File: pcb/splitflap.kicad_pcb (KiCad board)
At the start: 2 copper layers, 100 x 100 mm, 61 parts, among them J1 Conn_01x05, J10 Hall C, J11 Hall-D, J12 I2C, J2 Conn_01x05, J3 Conn_01x05, J4 Conn_01x05, J5 Barrel_Jack_Switch, J6 USB_C_Receptacle_USB2.0_16P, J7 Barrel_Jack_Switch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

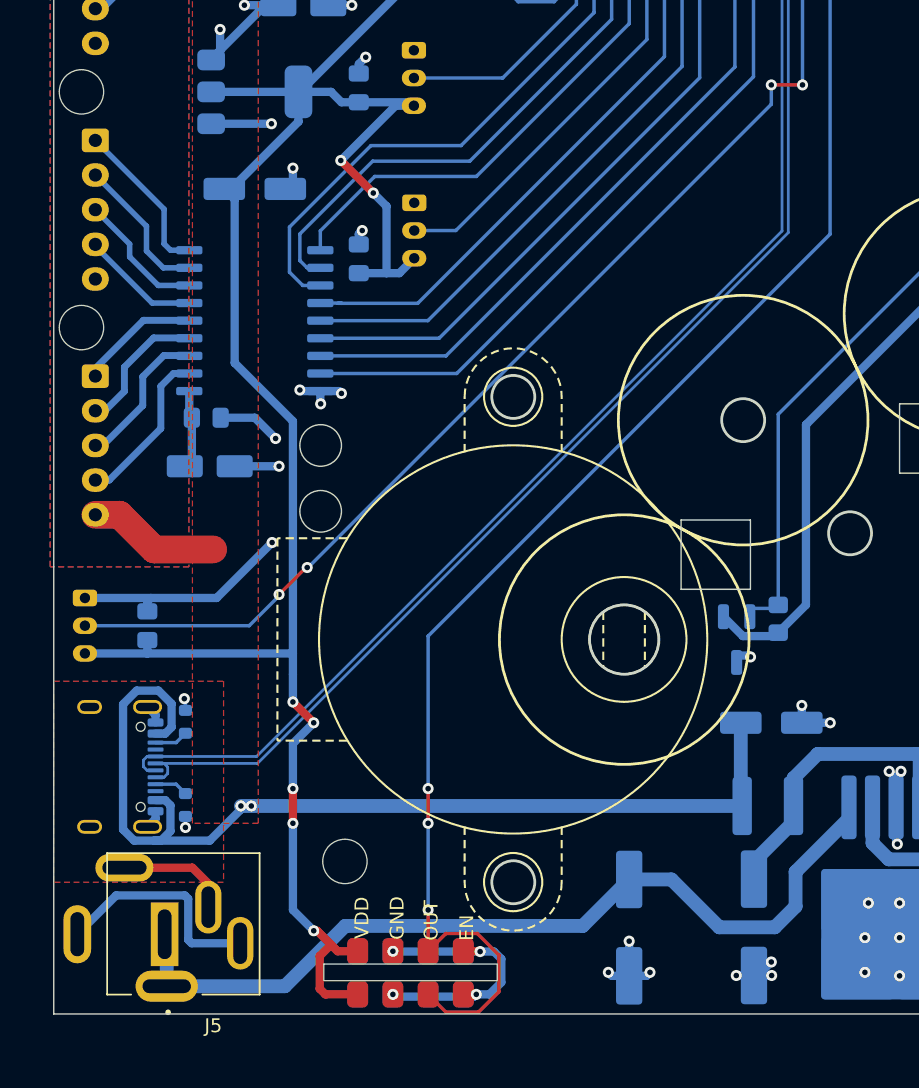
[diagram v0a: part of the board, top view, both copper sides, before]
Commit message: Add optional LED for DCF receiver
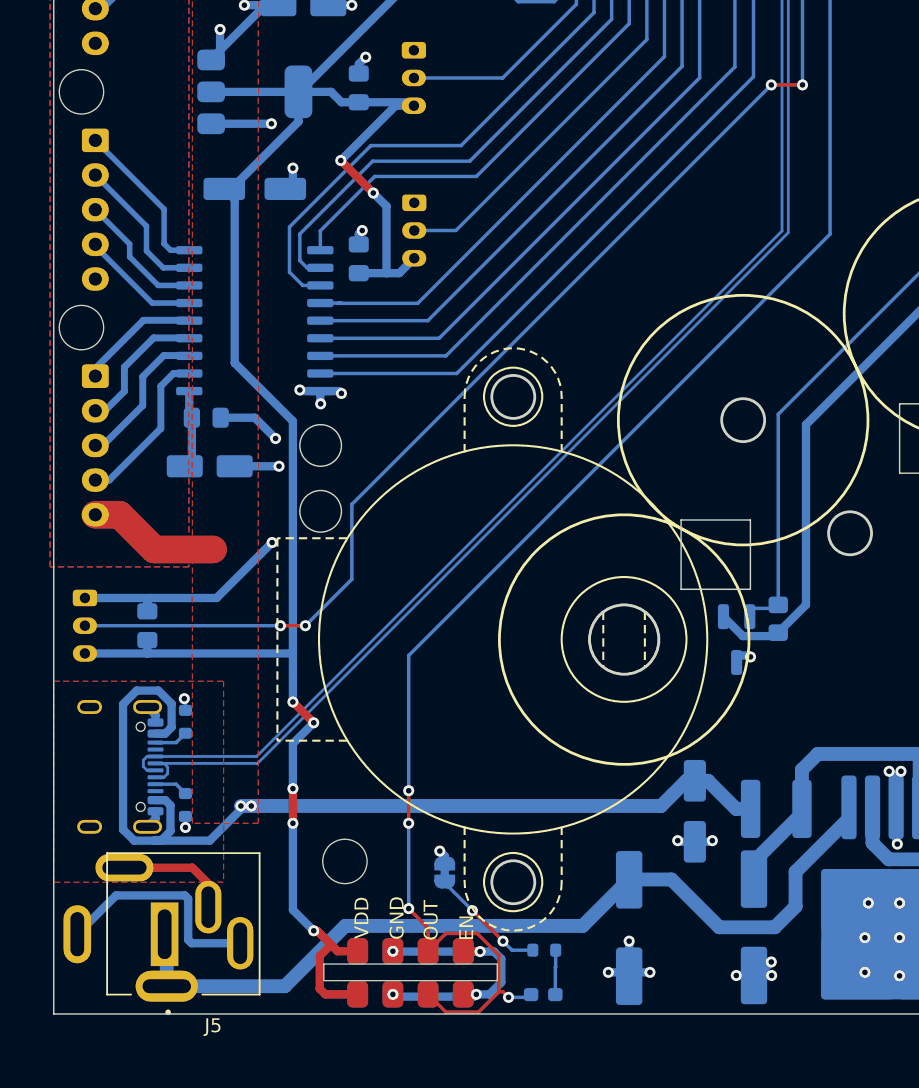
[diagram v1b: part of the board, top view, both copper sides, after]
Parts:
- added D2: LED, LED_SMD:LED_0603_1608Metric_Pad1.05x0.95mm_HandSolder, B.Cu at (135.3, 148.6)
- added JP2: DCF77 LED, Jumper:SolderJumper-2_P1.3mm_Bridged_RoundedPad1.0x1.5mm, B.Cu at (128.2, 139.8)
- added R6: 1k, Resistor_SMD:R_0603_1608Metric, B.Cu at (135.4, 145.4)
- moved C4 8.43 mm to (146.2, 135.4), turned to -90 degrees
- moved L2 0.64 mm to (152.1, 135.2)
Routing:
- net Net-(JP2-B): track 0.00 -> 8.46 mm, vias 0 -> 2
- net +5V: track 111.6 -> 107.7 mm
- net DCF77: track 114.9 -> 118.6 mm, vias 5 -> 6
- net Net-(D2-K): track 0.00 -> 3.21 mm
- net /HALL_A: track 122.8 -> 125.1 mm
- net GND: track 119.1 -> 119.5 mm, vias 53 -> 54

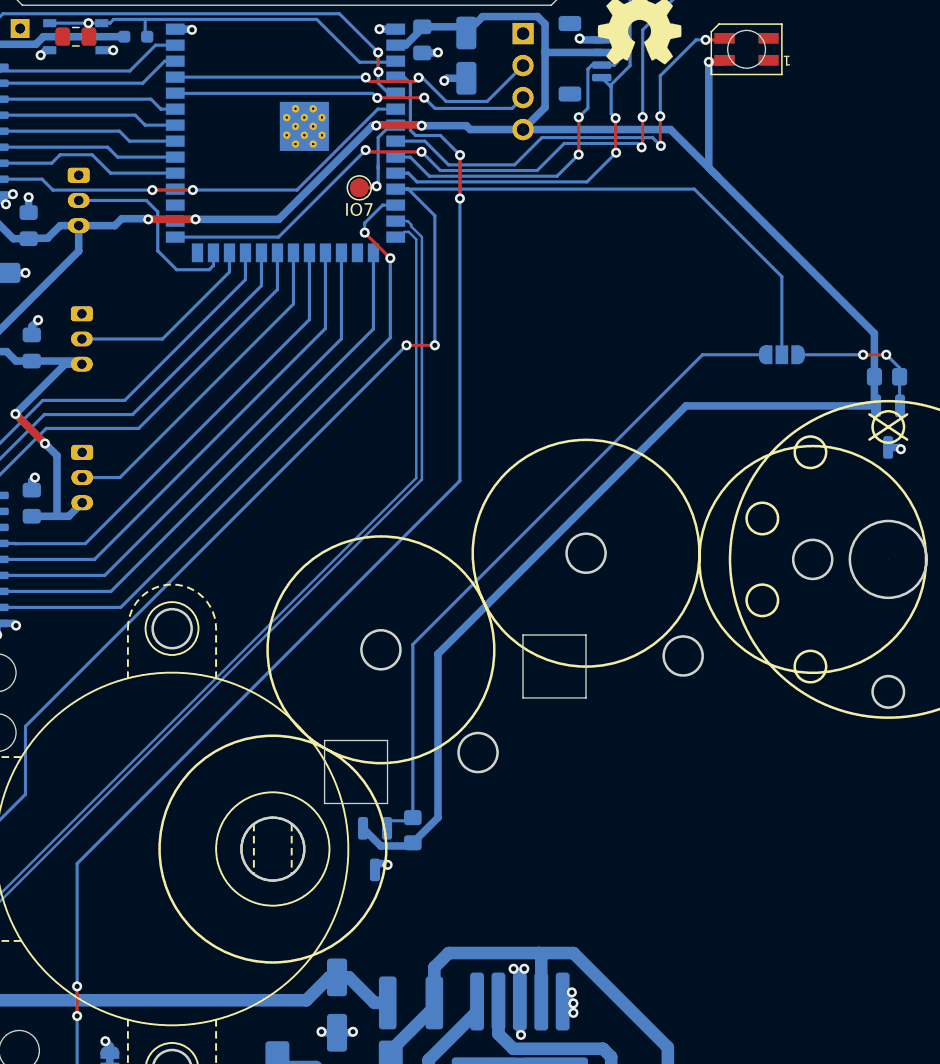
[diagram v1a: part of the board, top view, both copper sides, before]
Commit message: Add two Hall sensors to the current board so that the amount of backlash can be registered
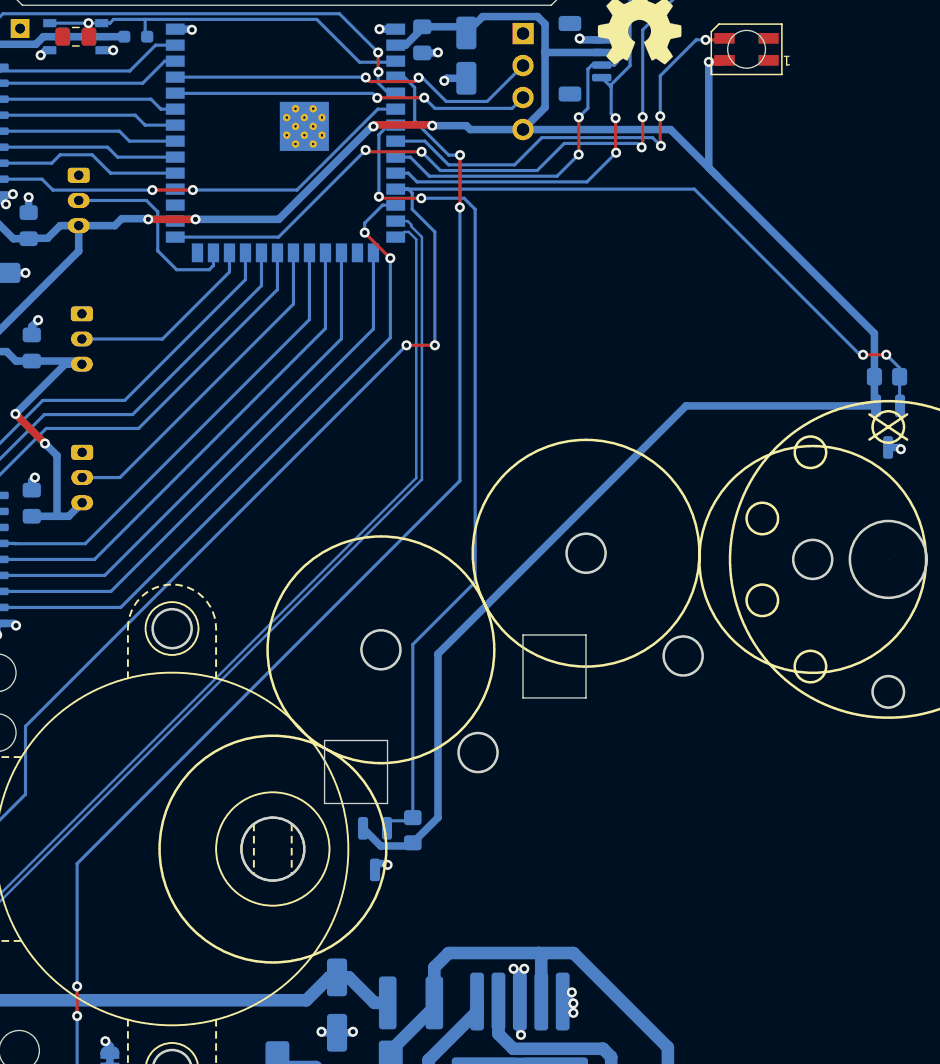
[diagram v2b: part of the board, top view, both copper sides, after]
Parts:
- removed JP1: Hall-A Switch, Jumper:SolderJumper-3_P1.3mm_Open_RoundedPad1.0x1.5mm
- removed TP1: IO7, TestPoint:TestPoint_Pad_D1.5mm
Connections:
- J8 pad 2: /HALL_A -> /HALL_A1
- U4 pad 11: /HALL_A -> /HALL_A1
- U4 pad 7: Extra -> /HALL_A2
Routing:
- net /HALL_A: track 125.1 -> 0.00 mm, vias 4 -> 0
- net /HALL_A1: track 11.5 -> 134.3 mm, vias 2 -> 6
- net /HALL_A2: track 53.5 -> 67.2 mm, vias 0 -> 2
- net Extra: track 7.40 -> 0.00 mm, vias 1 -> 0
- net DCF77: track 118.6 -> 118.0 mm

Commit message: Remapping the motors ABCD to match the connectors on the board
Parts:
- J1: value Conn_01x05 -> Motor D
- J11: value Hall-D -> Hall B
- J2: value Conn_01x05 -> Motor C
- J3: value Conn_01x05 -> Motor B
- J4: value Conn_01x05 -> Motor A
- J8: value Hall A -> Hall A1
- J9: value Hall B -> Hall D
- U5: value AH1815-W-7 -> Hall A1
- U9: value AH1815-W-7 -> Hall A2
- moved OSHW1 16.2 mm to (186.0, 61.6)
- moved C11 0.15 mm to (106.6, 122.0)
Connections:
- J1 pad 1: /MOUT-A1 -> /MOUT-D1
- J1 pad 2: /MOUT-A2 -> /MOUT-D2
- J1 pad 3: /MOUT-A3 -> /MOUT-D3
- J1 pad 4: /MOUT-A4 -> /MOUT-D4
- J11 pad 2: /HALL_D -> /HALL_B
- J2 pad 1: /MOUT-B1 -> /MOUT-C1
- J2 pad 2: /MOUT-B2 -> /MOUT-C2
- J2 pad 3: /MOUT-B3 -> /MOUT-C3
- J2 pad 4: /MOUT-B4 -> /MOUT-C4
- J3 pad 1: /MOUT-C1 -> /MOUT-B1
- J3 pad 2: /MOUT-C2 -> /MOUT-B2
- J3 pad 3: /MOUT-C3 -> /MOUT-B3
- J3 pad 4: /MOUT-C4 -> /MOUT-B4
- J4 pad 1: /MOUT-D1 -> /MOUT-A1
- J4 pad 2: /MOUT-D2 -> /MOUT-A2
- J4 pad 3: /MOUT-D3 -> /MOUT-A3
- J4 pad 4: /MOUT-D4 -> /MOUT-A4
- J9 pad 2: /HALL_B -> /HALL_D
- U1 pad 1: /MOTOR-A-1 -> /MOTOR-D-1
- U1 pad 11: /MOUT-B4 -> /MOUT-C4
- U1 pad 12: /MOUT-B3 -> /MOUT-C3
- U1 pad 13: /MOUT-B2 -> /MOUT-C2
- U1 pad 14: /MOUT-B1 -> /MOUT-C1
- U1 pad 15: /MOUT-A4 -> /MOUT-D4
- U1 pad 16: /MOUT-A3 -> /MOUT-D3
- U1 pad 17: /MOUT-A2 -> /MOUT-D2
- U1 pad 18: /MOUT-A1 -> /MOUT-D1
- U1 pad 2: /MOTOR-A-2 -> /MOTOR-D-2
- U1 pad 3: /MOTOR-A-3 -> /MOTOR-D-3
- U1 pad 4: /MOTOR-A-4 -> /MOTOR-D-4
- U1 pad 5: /MOTOR-B-1 -> /MOTOR-C-1
- U1 pad 6: /MOTOR-B-2 -> /MOTOR-C-2
- U1 pad 7: /MOTOR-B-3 -> /MOTOR-C-3
- U1 pad 8: /MOTOR-B-4 -> /MOTOR-C-4
- U2 pad 1: /MOTOR-C-1 -> /MOTOR-B-1
- U2 pad 11: /MOUT-D4 -> /MOUT-A4
- U2 pad 12: /MOUT-D3 -> /MOUT-A3
- U2 pad 13: /MOUT-D2 -> /MOUT-A2
- U2 pad 14: /MOUT-D1 -> /MOUT-A1
- U2 pad 15: /MOUT-C4 -> /MOUT-B4
- U2 pad 16: /MOUT-C3 -> /MOUT-B3
- U2 pad 17: /MOUT-C2 -> /MOUT-B2
- U2 pad 18: /MOUT-C1 -> /MOUT-B1
- U2 pad 2: /MOTOR-C-2 -> /MOTOR-B-2
- U2 pad 3: /MOTOR-C-3 -> /MOTOR-B-3
- U2 pad 4: /MOTOR-C-4 -> /MOTOR-B-4
- U2 pad 5: /MOTOR-D-1 -> /MOTOR-A-1
- U2 pad 6: /MOTOR-D-2 -> /MOTOR-A-2
- U2 pad 7: /MOTOR-D-3 -> /MOTOR-A-3
- U2 pad 8: /MOTOR-D-4 -> /MOTOR-A-4
- U4 pad 12: /MOTOR-D-4 -> /MOTOR-A-4
- U4 pad 15: /MOTOR-D-3 -> /MOTOR-A-3
- U4 pad 17: /MOTOR-D-2 -> /MOTOR-A-2
- U4 pad 18: /MOTOR-D-1 -> /MOTOR-A-1
- U4 pad 19: /MOTOR-C-4 -> /MOTOR-B-4
- U4 pad 20: /HALL_D -> /HALL_B
- U4 pad 21: /MOTOR-C-1 -> /MOTOR-B-1
- U4 pad 22: /MOTOR-C-2 -> /MOTOR-B-2
- U4 pad 23: /MOTOR-C-3 -> /MOTOR-B-3
- U4 pad 25: /HALL_B -> /HALL_D
- U4 pad 31: /MOTOR-B-3 -> /MOTOR-C-3
- U4 pad 32: /MOTOR-B-2 -> /MOTOR-C-2
- U4 pad 33: /MOTOR-B-1 -> /MOTOR-C-1
- U4 pad 34: /MOTOR-A-4 -> /MOTOR-D-4
- U4 pad 35: /MOTOR-A-3 -> /MOTOR-D-3
- U4 pad 38: /MOTOR-A-2 -> /MOTOR-D-2
- U4 pad 39: /MOTOR-A-1 -> /MOTOR-D-1
- U4 pad 6: /MOTOR-B-4 -> /MOTOR-C-4
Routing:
- net /MOTOR-D-4: track 53.1 -> 14.5 mm, vias 2 -> 0
- net /MOTOR-A-4: track 14.5 -> 53.1 mm, vias 0 -> 2
- net /MOTOR-D-3: track 44.6 -> 14.5 mm
- net /MOTOR-A-3: track 14.5 -> 44.6 mm
- net /MOTOR-D-2: track 42.0 -> 14.9 mm
- net /MOTOR-A-2: track 14.9 -> 42.0 mm
- net /MOTOR-D-1: track 39.7 -> 15.1 mm
- net /MOTOR-A-1: track 15.1 -> 39.7 mm
- net /MOTOR-C-3: track 36.4 -> 15.0 mm
- net /MOTOR-B-3: track 15.0 -> 36.4 mm
- net /MOTOR-C-2: track 35.1 -> 14.5 mm
- net /MOTOR-B-2: track 14.5 -> 35.1 mm
- net /MOTOR-C-1: track 32.8 -> 14.5 mm
- net /MOTOR-B-1: track 14.5 -> 32.8 mm
- net /HALL_D: track 26.5 -> 15.9 mm
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
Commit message: Add capacitors for hall sensors power pins
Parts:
- added C1: 100n, Capacitor_SMD:C_0805_2012Metric_Pad1.18x1.45mm_HandSolder, B.Cu at (187.0, 90.0)
- added C17: 100n, Capacitor_SMD:C_0805_2012Metric_Pad1.18x1.45mm_HandSolder, B.Cu at (153.2, 124.6)
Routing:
- net +3V3: track 361.1 -> 364.4 mm
- net GND: track 119.6 -> 121.8 mm, vias 54 -> 56

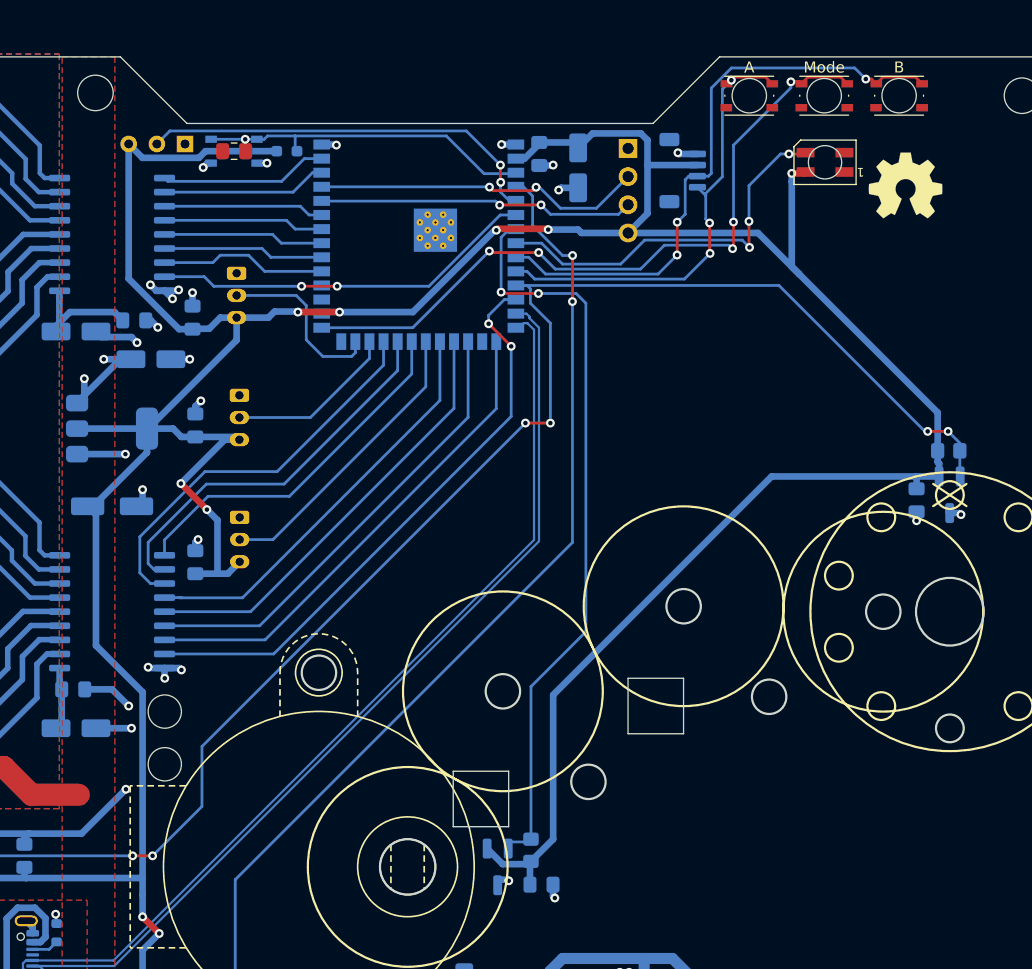
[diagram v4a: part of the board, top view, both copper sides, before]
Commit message: DNP components and bigger pads for hand solder items
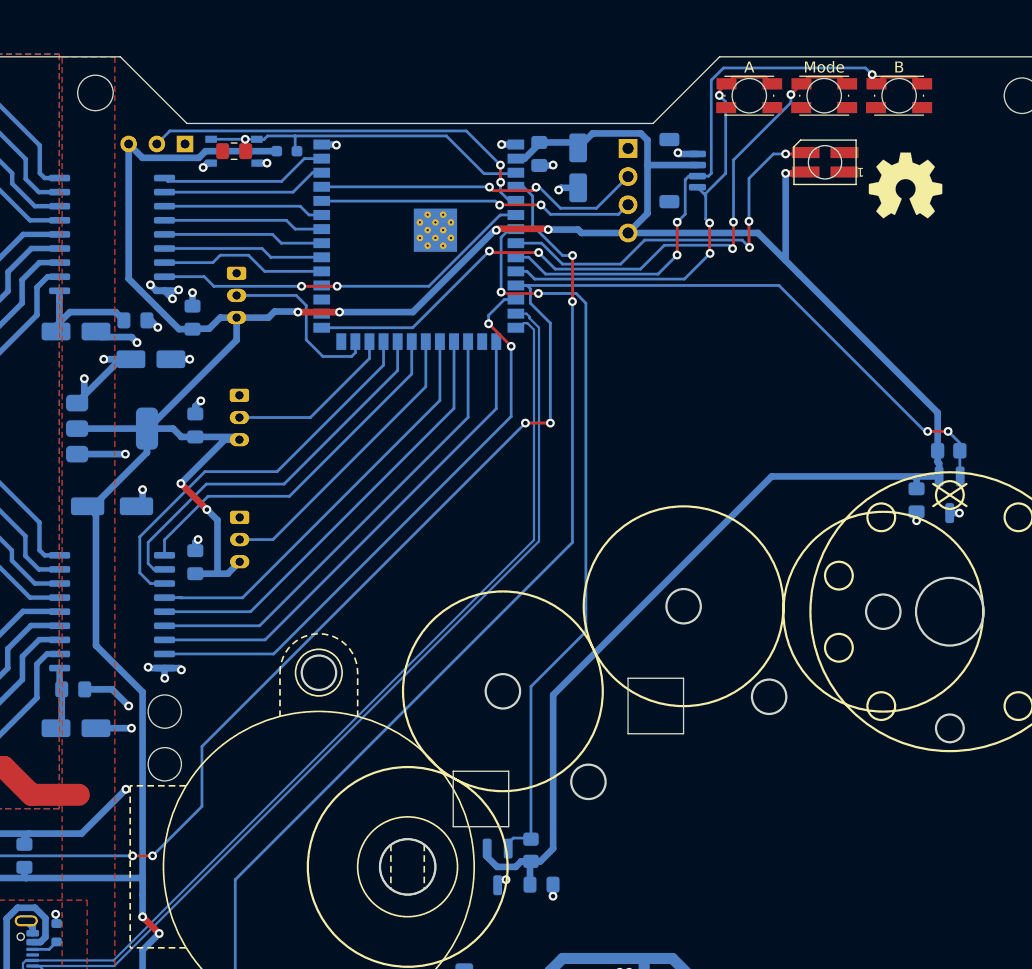
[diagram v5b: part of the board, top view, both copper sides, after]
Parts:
- J5: value Barrel_Jack_Switch -> BarrelJack Vertical
- J7: value Barrel_Jack_Switch -> BarrelJack Horizontal
- moved C10 0.10 mm to (116.6, 73.8)
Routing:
- net GND: track 121.8 -> 121.0 mm
- net /GPIO0: track 64.4 -> 63.6 mm
- net /SWB_SDA: track 54.1 -> 54.8 mm
- net /SWA_SCL: track 41.7 -> 41.1 mm

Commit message: Run DRC
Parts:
- moved J12 0.15 mm to (165.9, 60.4)
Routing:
- net GND: track 121.0 -> 120.1 mm
